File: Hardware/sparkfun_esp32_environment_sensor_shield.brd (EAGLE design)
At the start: 58.4 x 50.8 mm, 48 parts, among them J1 WEATHER_METER-WIND, J2 WEATHER_METER-RAIN, U1 BME280, U2 CCS811, U3 TSL2561FN, U4 ESD Diode

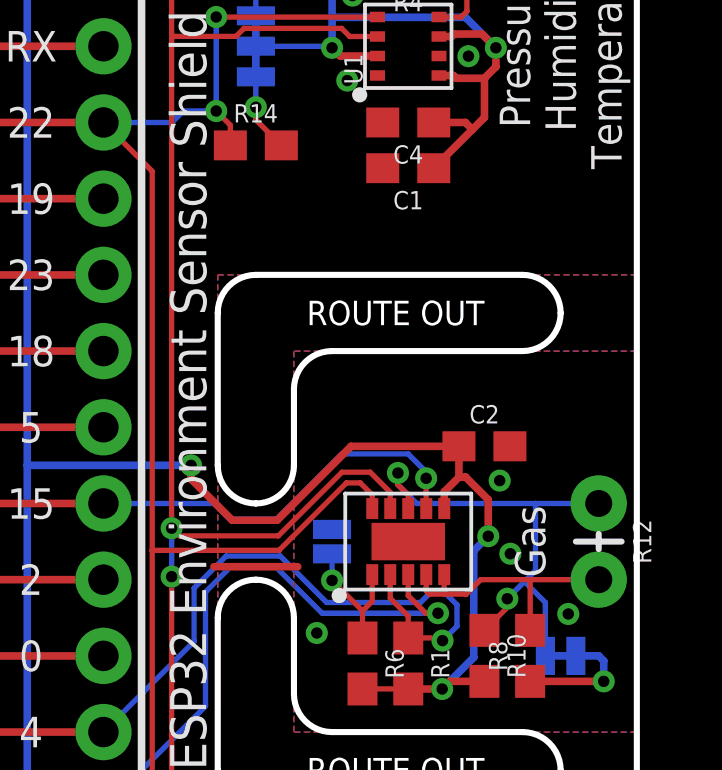
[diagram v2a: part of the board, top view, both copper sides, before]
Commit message: Post-review fixes: CCS811 paste, spell check
- Reduced size of CCS811's exposed pad paste aperature
- Fixed anemometer spelling
- Changed "Gas" to "Air" labels
- Clean up schematic
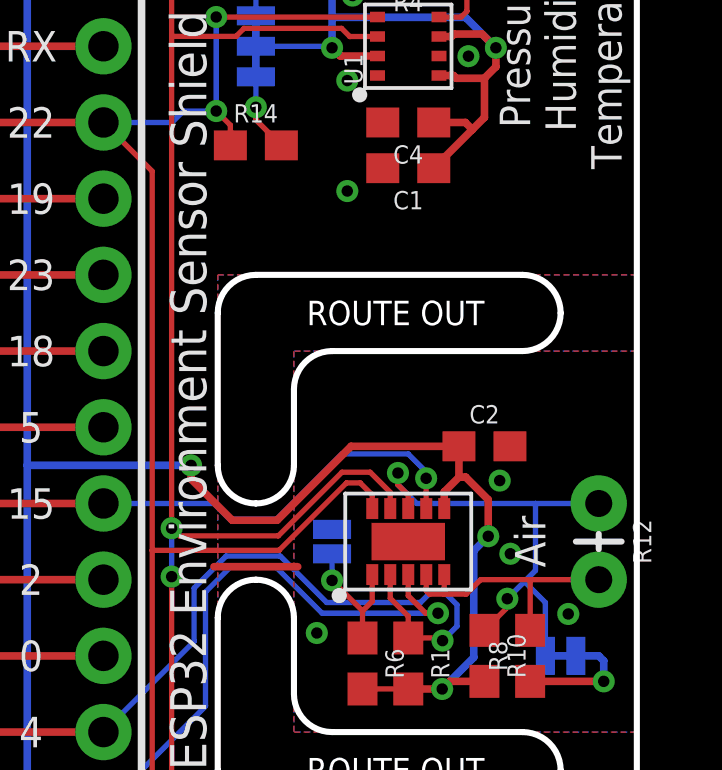
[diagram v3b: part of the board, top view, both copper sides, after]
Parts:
- R12: value DNP -> 10k
- U4: value ESD Diode -> TVS Diode
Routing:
- net GND: vias 10 -> 11
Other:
- board text added: "AIR !INT!"
- board text added: "AIR !RST!"
- board text added: "AIR !WAKE!"
- board text added: "Air"
- board text removed: "GAS !INT!"
- board text removed: "GAS !RST!"
- board text removed: "GAS !WAKE!"
- board text removed: "Gas"
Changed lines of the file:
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@@
 <layer number="47" name="Measures" color="7" fill="1" visible="no" active="yes"/>
 <layer number="48" name="Document" color="7" fill="1" visible="no" active="yes"/>
-<layer number="49" name="Reference" color="7" fill="1" visible="no" active="yes"/>
+<layer number="49" name="Reference" color="7" fill="1" visible="yes" active="yes"/>
 <layer number="50" name="dxf" color="7" fill="1" visible="no" active="no"/>
 <layer number="51" name="tDocu" color="6" fill="1" visible="yes" active="yes"/>
@@
 <text x="50.8" y="2.794" size="1.016" layer="21" font="vector" ratio="15" rot="R90" align="center-left">GND</text>
 <text x="54.864" y="10.16" size="1.016" layer="21" font="vector" ratio="15" rot="R270" align="bottom-center">Light</text>
-<text x="54.356" y="25.4" size="1.016" layer="21" font="vector" ratio="15" rot="R270" align="bottom-center">Gas</text>
+<text x="54.356" y="25.4" size="1.016" layer="21" font="vector" ratio="15" rot="R270" align="bottom-center">Air</text>
 <text x="53.848" y="41.91" size="1.016" layer="21" font="vector" ratio="15" rot="R90" align="top-center">Pressure
 Humidity
@@
 <text x="55.88" y="25.4" size="0.889" layer="22" ratio="15" rot="MR270" align="bottom-center">10kΩ
 NTC</text>
-<text x="41.783" y="16.51" size="0.889" layer="22" font="vector" ratio="15" rot="MR0" align="center-right">GAS
+<text x="41.783" y="16.51" size="0.889" layer="22" font="vector" ratio="15" rot="MR0" align="center-right">AIR
 !INT!</text>
 <text x="41.656" y="13.97" size="0.889" layer="22" font="vector" ratio="15" rot="MR0" align="center-right">LUX
 !INT!</text>
-<text x="41.783" y="19.05" size="0.889" layer="22" font="vector" ratio="15" rot="MR0" align="center-right">GAS
+<text x="41.783" y="19.05" size="0.889" layer="22" font="vector" ratio="15" rot="MR0" align="center-right">AIR
 !RST!</text>
-<text x="41.783" y="26.67" size="0.889" layer="22" font="vector" ratio="15" rot="MR0" align="center-right">GAS
+<text x="41.783" y="26.67" size="0.889" layer="22" font="vector" ratio="15" rot="MR0" align="center-right">AIR
 !WAKE!</text>
 <text x="41.783" y="39.37" size="0.889" layer="22" font="vector" ratio="15" rot="MR0" align="center-right">SCL</text>
@@
 <element name="FRAME1" library="SparkFun-Aesthetics" package="CREATIVE_COMMONS" value="FRAME-LETTER" x="-13.97" y="-21.59"/>
 <element name="U2" library="esp32-environ-monitor-temp" package="LGA10-2.7X4.0MM" value="CCS811" x="50.8" y="25.4" rot="R90">
-<attribute name="PROD_ID" value="TBD" x="50.8" y="25.4" size="1.778" layer="27" font="vector" ratio="15" rot="R90" display="off"/>
+<attribute name="PROD_ID" value="IC-13607" x="50.8" y="25.4" size="1.778" layer="27" font="vector" ratio="15" rot="R90" display="off"/>
 </element>
 <element name="J8" library="SparkFun-Connectors" package="1X04" value="" x="50.8" y="1.27" rot="R180"/>
@@
 <element name="JP5" library="SparkFun-Jumpers" package="SMT-JUMPER_3_2-NC_TRACE_SILK" value="" x="45.72" y="41.91" rot="MR90"/>
 <element name="R8" library="esp32-environ-monitor-temp" package="0603" value="10k" x="54.864" y="21.59" rot="R90">
-<attribute name="PROD_ID" value="TBD" x="54.864" y="21.59" size="1.778" layer="27" rot="R90" display="off"/>
+<attribute name="PROD_ID" value="RES-13608" x="54.864" y="21.59" size="1.778" layer="27" rot="R90" display="off"/>
 <attribute name="VALUE" value="10k" x="54.864" y="21.59" size="1.778" layer="27" rot="R90" display="off"/>
 </element>
-<element name="R12" library="esp32-environ-monitor-temp" package="AXIAL-0.1" value="DNP" x="57.15" y="25.4" rot="R270">
+<element name="R12" library="esp32-environ-monitor-temp" package="AXIAL-0.1" value="10k" x="57.15" y="25.4" rot="R270">
 <attribute name="PROD_ID" value="TBD" x="57.15" y="25.4" size="0.8128" layer="27" ratio="15" rot="R270" display="off"/>
 <attribute name="SF_ID" value="SEN-00250" x="57.15" y="25.4" size="1.778" layer="27" rot="R270" display="off"/>
@@
 <element name="FD1" library="SparkFun-Aesthetics" package="FIDUCIAL-1X2" value="FIDUCIAL1X2" x="6.35" y="48.26"/>
 <element name="FD2" library="SparkFun-Aesthetics" package="FIDUCIAL-1X2" value="FIDUCIAL1X2" x="57.15" y="6.35"/>
-<element name="U4" library="esp32-environ-monitor-temp" package="SOT-23-6" value="ESD Diode" x="12.7" y="25.4" rot="R270">
+<element name="U4" library="esp32-environ-monitor-temp" package="SOT-23-6" value="TVS Diode" x="12.7" y="25.4" rot="R270">
 <attribute name="PROD_ID" value="IC-13538" x="12.7" y="25.4" size="0.889" layer="27" font="vector" ratio="15" rot="R270" display="off"/>
 </element>
@@
 <contactref element="U4" pad="2"/>
 <via x="9.779" y="25.4" extent="1-16" drill="0.381"/>
+<via x="48.768" y="37.084" extent="1-16" drill="0.381"/>
 </signal>
 <signal name="SCL">

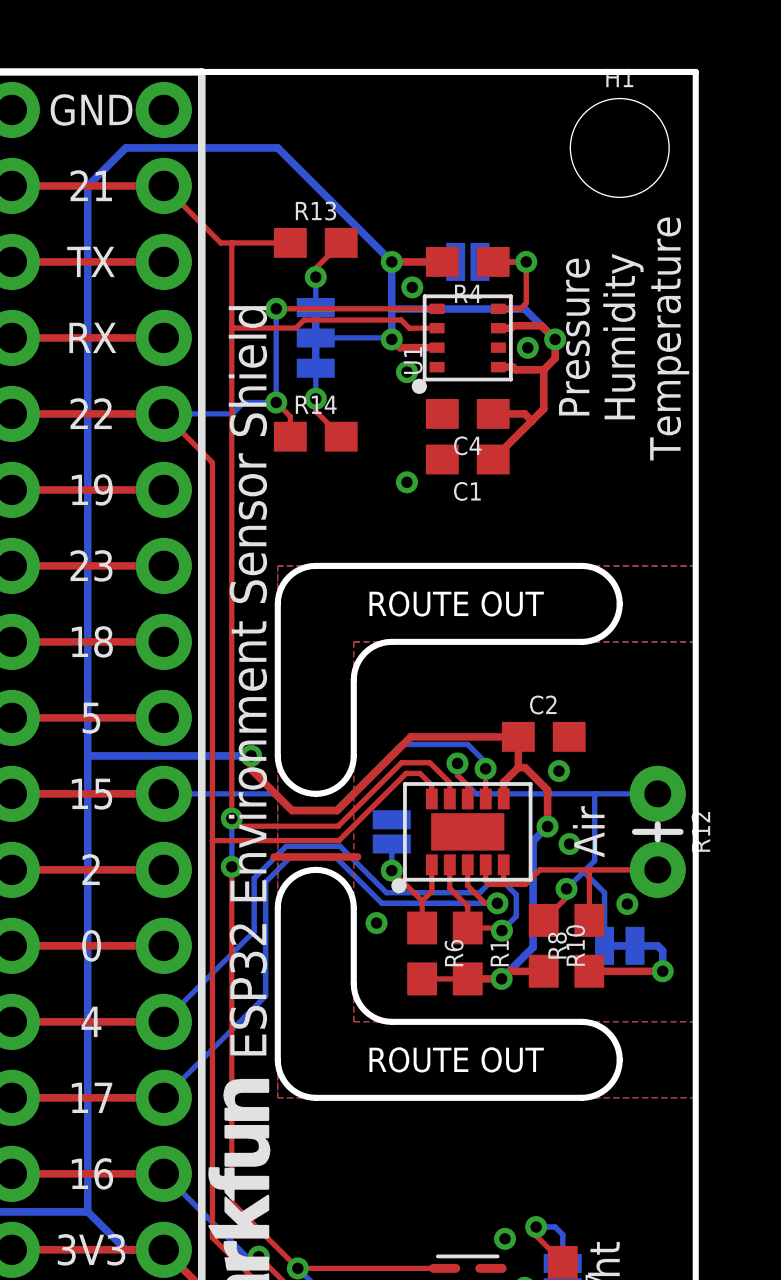
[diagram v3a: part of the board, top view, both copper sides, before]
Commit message: Minor adjustments after running Engineer checklist.
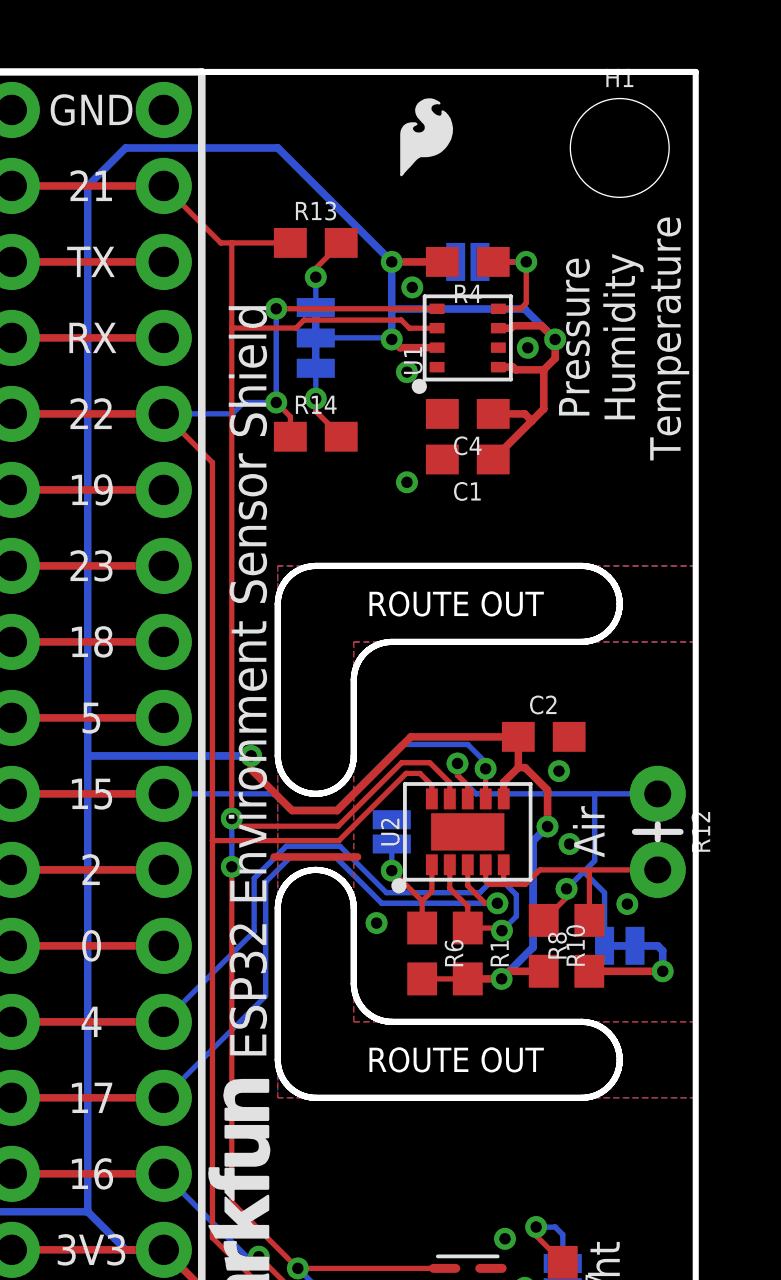
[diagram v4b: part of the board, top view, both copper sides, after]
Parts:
- added LOGO3: SFE_LOGO_FLAME.1_INCH, SparkFun-Aesthetics:SFE_LOGO_FLAME_.1
- R12: value 10k -> DNP
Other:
- outline, holes or cut-outs redrawn
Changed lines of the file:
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@@
 DIR</text>
 <text x="16.51" y="26.67" size="0.889" layer="22" font="vector" ratio="15" rot="MR0" align="center-left">SOIL</text>
+<dimension x1="0" y1="0" x2="0" y2="50.8" x3="-7.62" y3="25.4" textsize="0.889" textratio="15" layer="47" dtype="vertical" unit="inch" precision="3"/>
+<dimension x1="2.54" y1="48.26" x2="2.54" y2="0" x3="-5.08" y3="24.13" textsize="0.889" textratio="15" layer="47" dtype="vertical" unit="inch" precision="3"/>
+<dimension x1="2.54" y1="2.54" x2="-2.54" y2="0" x3="-2.54" y3="1.27" textsize="0.889" textratio="15" layer="47" dtype="vertical" unit="inch" precision="3"/>
+<dimension x1="58.42" y1="0" x2="0" y2="0" x3="29.21" y3="-7.62" textsize="0.889" textratio="15" layer="47" dtype="horizontal" unit="inch" precision="3"/>
+<dimension x1="55.88" y1="2.54" x2="0" y2="2.54" x3="27.94" y3="-5.08" textsize="0.889" textratio="15" layer="47" dtype="horizontal" unit="inch" precision="3"/>
+<dimension x1="2.54" y1="2.54" x2="0" y2="2.54" x3="1.27" y3="-2.54" textsize="0.889" textratio="15" layer="47" dtype="horizontal" unit="inch" precision="3"/>
+<polygon width="0.2032" layer="46">
+<vertex x="45.72" y="26.67" curve="90"/>
+<vertex x="46.99" y="27.94"/>
+<vertex x="46.99" y="30.48" curve="-90"/>
+<vertex x="48.26" y="31.75"/>
+<vertex x="54.61" y="31.75" curve="90"/>
+<vertex x="55.88" y="33.02" curve="90"/>
+<vertex x="54.61" y="34.29"/>
+<vertex x="45.72" y="34.29" curve="90"/>
+<vertex x="44.45" y="33.02"/>
+<vertex x="44.45" y="27.94" curve="90"/>
+</polygon>
+<polygon width="0.2032" layer="46">
+<vertex x="45.72" y="24.13" curve="-90"/>
+<vertex x="46.99" y="22.86"/>
+<vertex x="46.99" y="20.32" curve="90"/>
+<vertex x="48.26" y="19.05"/>
+<vertex x="54.61" y="19.05" curve="-90"/>
+<vertex x="55.88" y="17.78" curve="-90"/>
+<vertex x="54.61" y="16.51"/>
+<vertex x="45.72" y="16.51" curve="-90"/>
+<vertex x="44.45" y="17.78"/>
+<vertex x="44.45" y="22.86" curve="-90"/>
+</polygon>
 </plain>
 <attributes>
@@
 <element name="JP4" library="SparkFun-Jumpers" package="SMT-JUMPER_2_NC_TRACE_SILK" value="" x="55.88" y="21.59" rot="MR0"/>
 <element name="J2" library="esp32-environ-monitor-temp" package="RJ11-6" value="WEATHER_METER-RAIN" x="5.08" y="12.7" rot="R270">
-<attribute name="PROD_ID" value="COMP-13401" x="25.4" y="26.67" size="1.778" layer="27" font="vector" ratio="15" rot="R270" display="off"/>
+<attribute name="PROD_ID" value="CONN-08590" x="25.4" y="26.67" size="1.778" layer="27" font="vector" ratio="15" rot="R270" display="off"/>
 <attribute name="SF_ID" value="SEN-08942" x="25.4" y="26.67" size="1.778" layer="27" font="vector" ratio="15" rot="R270" display="off"/>
 </element>
@@
 <attribute name="VALUE" value="10k" x="54.864" y="21.59" size="1.778" layer="27" rot="R90" display="off"/>
 </element>
-<element name="R12" library="esp32-environ-monitor-temp" package="AXIAL-0.1" value="10k" x="57.15" y="25.4" rot="R270">
-<attribute name="PROD_ID" value="TBD" x="57.15" y="25.4" size="0.8128" layer="27" ratio="15" rot="R270" display="off"/>
+<element name="R12" library="esp32-environ-monitor-temp" package="AXIAL-0.1" value="DNP" x="57.15" y="25.4" rot="R270">
+<attribute name="PROD_ID" value="N/A" x="57.15" y="25.4" size="0.8128" layer="27" ratio="15" rot="R270" display="off"/>
 <attribute name="SF_ID" value="SEN-00250" x="57.15" y="25.4" size="1.778" layer="27" rot="R270" display="off"/>
 </element>
@@
 <attribute name="PROD_ID" value="IC-13538" x="12.7" y="25.4" size="0.889" layer="27" font="vector" ratio="15" rot="R270" display="off"/>
 </element>
+<element name="LOGO3" library="SparkFun-Aesthetics" package="SFE_LOGO_FLAME_.1" value="SFE_LOGO_FLAME.1_INCH" x="48.26" y="46.99"/>
 </elements>
 <signals>
 <signal name="GND">
-<contactref element="B1" pad="1"/>
-<contactref element="B1" pad="40"/>
-<contactref element="B1" pad="4"/>
-<contactref element="B1" pad="37"/>
-<contactref element="B1" pad="21"/>
 <polygon width="0.254" layer="1" isolate="0.1778">
 <vertex x="0" y="0"/>
@@
 <contactref element="J1" pad="3"/>
 <contactref element="J3" pad="1"/>
-<contactref element="J4" pad="1"/>
-<contactref element="J4" pad="4"/>
-<contactref element="J13" pad="1"/>
-<contactref element="J13" pad="4"/>
-<contactref element="J13" pad="20"/>
 <via x="47.752" y="22.352" extent="1-16" drill="0.381"/>
 <via x="53.848" y="27.432" extent="1-16" drill="0.381"/>
@@
 <via x="9.779" y="25.4" extent="1-16" drill="0.381"/>
 <via x="48.768" y="37.084" extent="1-16" drill="0.381"/>
+<contactref element="B1" pad="1"/>
+<contactref element="B1" pad="4"/>
+<contactref element="J4" pad="1"/>
+<contactref element="J4" pad="4"/>
+<contactref element="B1" pad="40"/>
+<contactref element="J13" pad="1"/>
+<contactref element="B1" pad="37"/>
+<contactref element="J13" pad="4"/>
+<contactref element="B1" pad="21"/>
+<contactref element="J13" pad="20"/>
 </signal>
 <signal name="SCL">
